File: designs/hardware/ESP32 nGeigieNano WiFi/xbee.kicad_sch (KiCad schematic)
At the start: 9 parts, among them SW1 TACT-SWITCH, SW2 SWITCH_INV, U1 ESP32S, U2 XBEE-socket

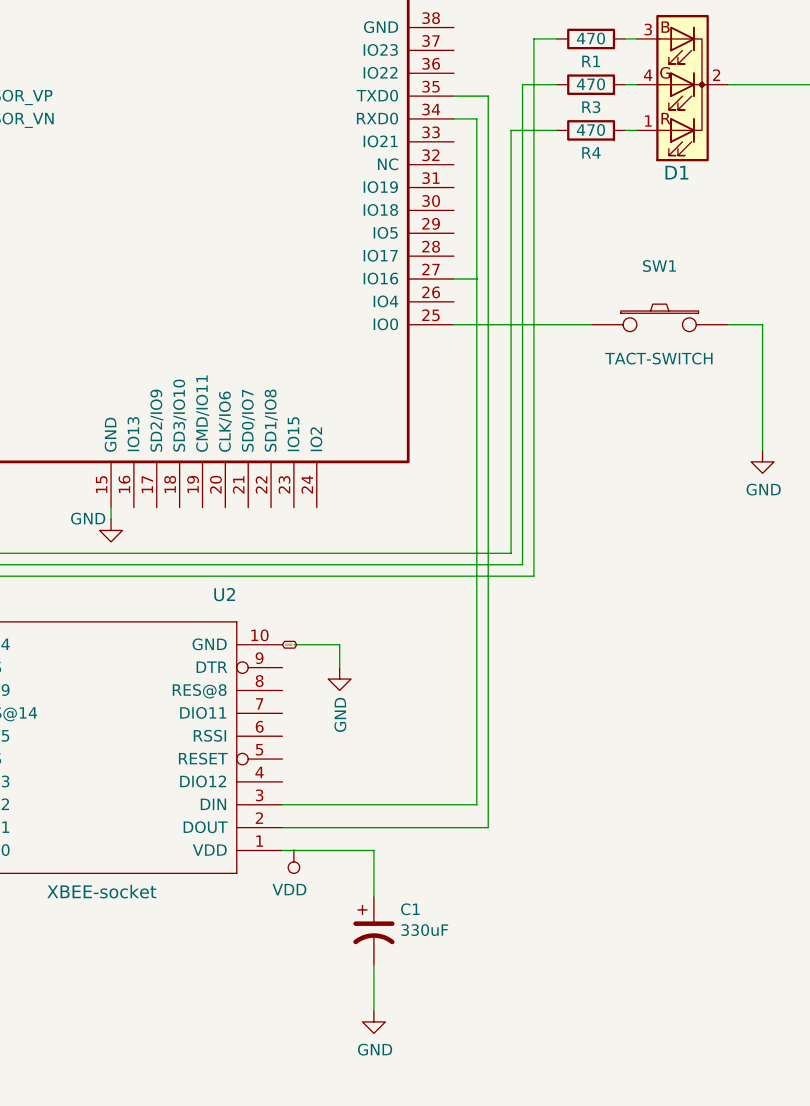
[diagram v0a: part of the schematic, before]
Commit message: Updated 3d models for board
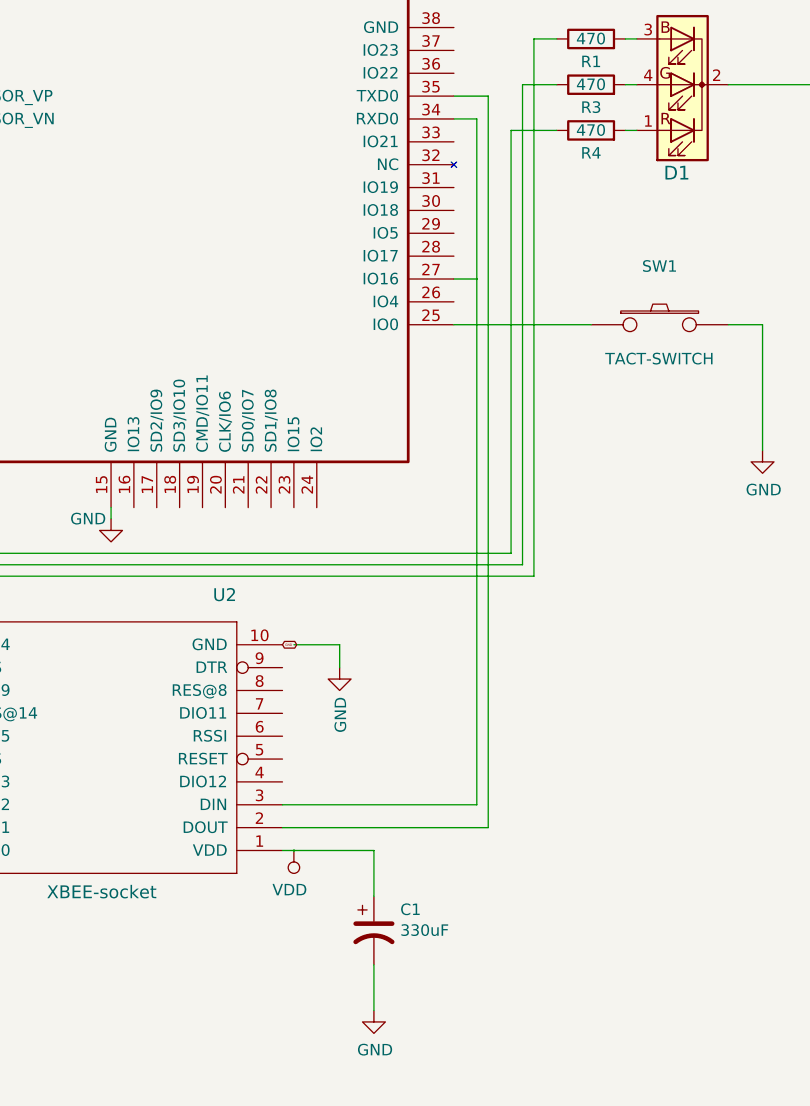
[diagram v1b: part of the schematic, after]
